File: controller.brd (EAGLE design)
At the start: 49.8 x 50 mm, 26 parts, among them SW1 EC12E_SW, U1 LCD-16X2NOHOLES

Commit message: Simplified controller design, internal arduino pullup resistors can be used.
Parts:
- removed R2: 47k, rcl:M0805
- removed R4, R5: 100R, rcl:M0805
- removed RN1: 10k, resistor-dil:0603-ARC
- moved C1 48.8 mm to (32.0, 13.0), flipped to the bottom, turned to 90 degrees
- moved R3 26.1 mm to (12.0, 15.0), flipped to the bottom
- moved C10 14.3 mm to (37.0, 26.0)
- moved C8 14.2 mm to (28.0, 43.0), turned to 180 degrees
- moved C11 5.00 mm to (31.0, 38.0), turned to 180 degrees
- moved C15 2.83 mm to (25.0, 38.0)
- moved S1 1.58 mm to (13.5, 41.0), turned to 0 degrees
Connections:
- removed net N$13: IO2.2, R5.2
- removed net SENSOR1: IO1.2, R4.2
- new net V+: POWER.2, R1.1, U1.2
- net +5V: no longer PHOTOCELL.2, POWER.2, R1.1, RN1.5, RN1.6, RN1.7, RN1.8, U1.2
- net EXTRA_IO1: now also IO1.2; no longer R4.1
- net EXTRA_IO2: now also IO2.2; no longer R5.1
- net GND: now also PHOTOCELL.1; no longer R2.1
- net LIGHTLEVEL: now also PHOTOCELL.2; no longer PHOTOCELL.1, R2.2
- net ROTARY_A: no longer RN1.3
- net ROTARY_B: no longer RN1.4
- net ROTARY_PUSH: no longer RN1.2
- net SHAKE_SENSOR: no longer RN1.1
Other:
- board text added: "TODO: Check size of * Radio module And make sure they can be mounted at the same time (on top?)."
- board text removed: "TODO: Check size of * Sound sensor module * Radio module * PIR module And make sure they can be mounted at the same time (on top?)."

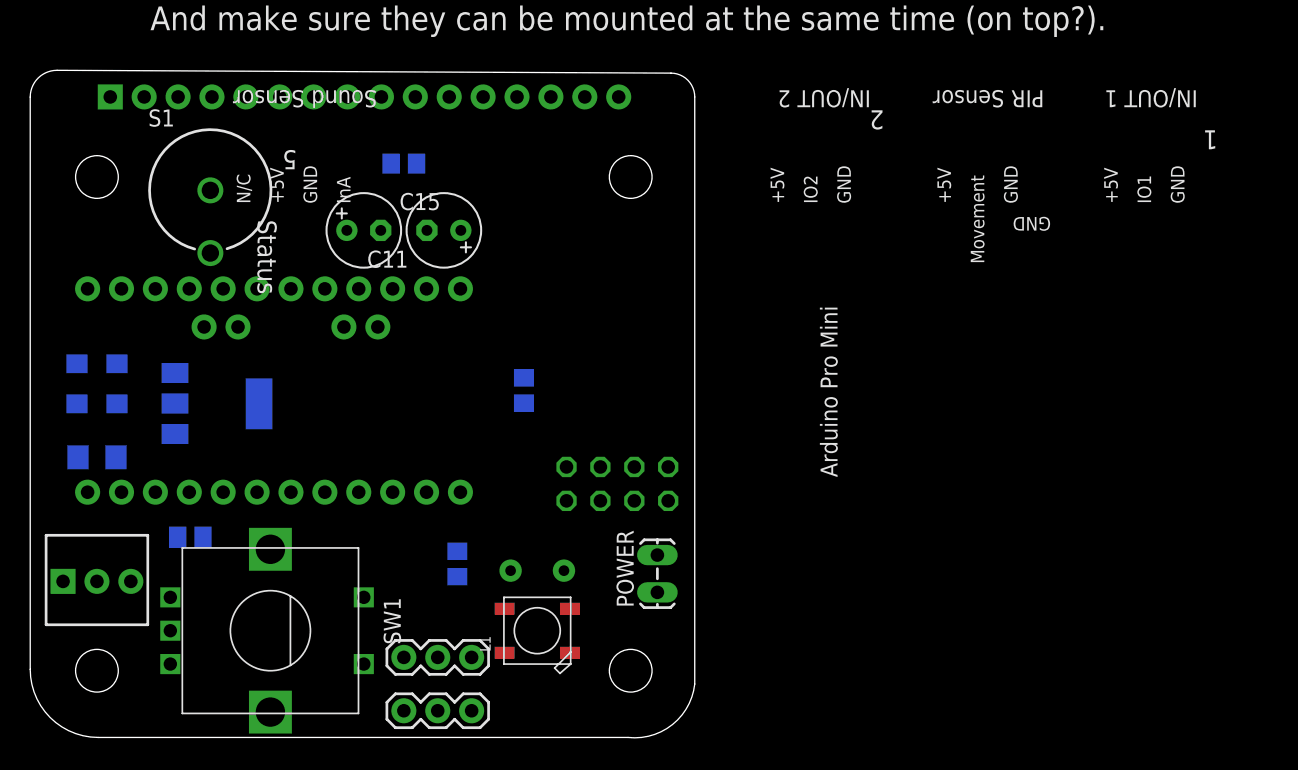
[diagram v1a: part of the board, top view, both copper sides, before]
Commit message: Working on controller board. Simplified scamea a bit.
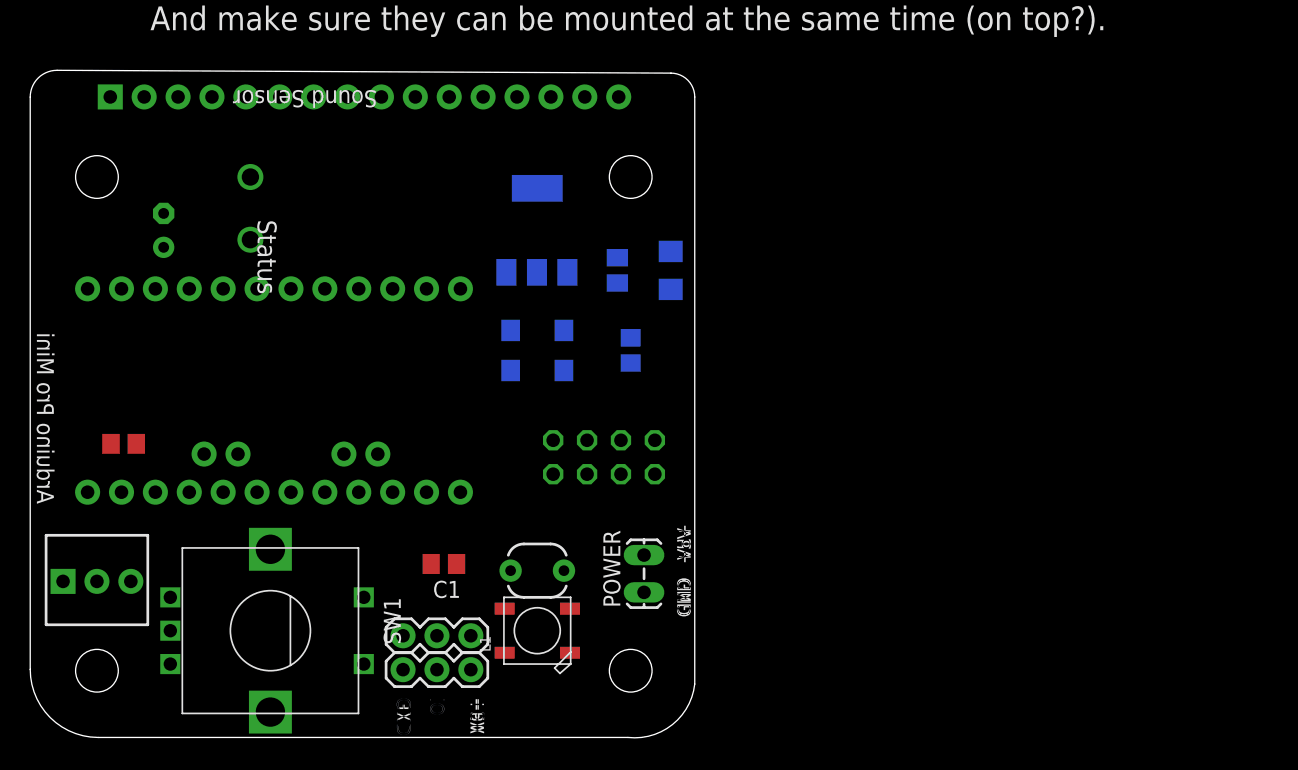
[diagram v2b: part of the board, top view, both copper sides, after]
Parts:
- removed C11: 100 uF, rcl:E2,5-6
- moved POWERLED 45.2 mm to (48.0, 35.0), turned to 90 degrees
- moved LOGO3 44.4 mm to (27.5, 39.5)
- moved R3 37.7 mm to (44.0, 35.0), turned to 90 degrees
- moved C12 35.2 mm to (40.0, 29.0), turned to 270 degrees
- moved C13 31.0 mm to (36.0, 29.0), turned to 270 degrees
- moved C8 29.7 mm to (7.00, 22.0), flipped to the top
- moved 3.3V_REGULATOR 27.3 mm to (38.0, 38.0), turned to 0 degrees
- moved C15 15.0 mm to (10.0, 38.0), flipped to the bottom, turned to 90 degrees
- moved C10 8.54 mm to (45.0, 29.0), turned to 270 degrees
- moved S1 3.16 mm to (16.5, 42.0), flipped to the bottom
- moved IO2 3.08 mm to (27.9, 5.08)
- moved RADIO 2.24 mm to (43.0, 21.0)
- moved IO1 1.62 mm to (27.9, 7.62)
- moved C1 1.00 mm to (31.0, 13.0), flipped to the top, turned to 180 degrees
- moved POWER 1.00 mm to (46.0, 11.0)
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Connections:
- net +3V3: no longer C11.+
- net GND: no longer C11.-
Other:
- board text added: "IO"
- board text added: "LedController v0.3"
- board text removed: "1"
- board text removed: "2"
- board text removed: "5"
- board text removed: "IN/OUT 1"
- board text removed: "IN/OUT 2"
- board text removed: "IO1"
- board text removed: "IO2"
- board text removed: "InA"
- board text removed: "LEDMess Node v2.0"
- board text removed: "Movement"
- board text removed: "N/C"
- board text removed: "PIR Sensor"
- board text removed: "RST"
- board text removed: "RXI"
- board text removed: "TXO"
